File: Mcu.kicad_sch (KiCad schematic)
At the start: 28 parts, among them J10 AUX2, J8 AUX0, J9 AUX1, U7 STM32H723VGHx, X2 X322516MLB4SI

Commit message: Started discrete inverter version
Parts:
- added U12: STM32H723VGT6, LQFP100_STM, symbol 2026-08-10_19-26-15:STM32H723VGT6
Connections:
- net AN_DRV_SO_A: now also U12.30 (PA6); no longer U7.J3 (PA6)
- net AN_DRV_SO_B: now also U12.31 (PA7); no longer U7.K3 (PA7)
- net AN_DRV_SO_C: now also U12.35 (PB1); no longer U7.K4 (PB1)
- net AN_EXT_IN_0: now also U12.25 (PA3); no longer U7.K2 (PA3)
- net AN_EXT_IN_1: now also U12.15 (PC0); no longer U7.F1 (PC0)
- net AN_VBUS: now also U12.24 (PA2); no longer U7.J2 (PA2)
- net CAN_RX: now also U12.81 (PD0); no longer U7.D8 (PD0)
- net CAN_TX: now also U12.82 (PD1); no longer U7.E8 (PD1)
- net DEBUG_RX: now also U12.80 (PC12); no longer U7.C8 (PC12)
- net DEBUG_TX: now also U12.83 (PD2); no longer U7.B7 (PD2)
- net DRV_AN_REF: now also U12.16 (PC1); no longer U7.F2 (PC1)
- net DRV_OFF: now also U12.47 (PB11); no longer U7.K7 (PB11)
- net DRV_SPI_CLK: now also U12.84 (PD3); no longer U7.C7 (PD3)
- net DRV_SPI_SDI: now also U12.18 (PC3_C); no longer U7.F3 (PC3_C)
- net DRV_SPI_SDO: now also U12.17 (PC2_C); no longer U7.E2 (PC2_C)
- net DRV_SPI_~{SCS}: now also U12.96 (PB9); no longer U7.A4 (PB9)
- net ENC_CLK: now also U12.89 (PB3); no longer U7.A7 (PB3(JTDO)
- net ENC_CS: now also U12.28 (PA4); no longer U7.G3 (PA4)
- net ENC_MISO: now also U12.90 (PB4); no longer U7.A6 (PB4(NJTRST))
- net ENC_MOSI: now also U12.91 (PB5); no longer U7.C5 (PB5)
- net GND: now also U12.10 (VSS), U12.26 (VSS); no longer U7.C2 (VSS), U7.E4 (VSS), U7.E5 (VSS), U7.E6 (VSS), U7.G1 (VSSA), U7.J1 (VSS)
- net NRST: now also U12.14 (NRST); no longer U7.E1 (NRST)
- net PA10: now also U12.69 (PA10); no longer U7.D10 (PA10)
- net PA5: now also U12.29 (PA5); no longer U7.H3 (PA5)
- net PA8: now also U12.67 (PA8); no longer U7.D9 (PA8)
- net PA9: now also U12.68 (PA9); no longer U7.C9 (PA9)
- net PB10: now also U12.46 (PB10); no longer U7.J7 (PB10)
- net PB12: now also U12.51 (PB12); no longer U7.K8 (PB12)
- net PB13: now also U12.52 (PB13); no longer U7.J8 (PB13)
- net PB14: now also U12.53 (PB14); no longer U7.H10 (PB14)
- net PB15: now also U12.54 (PB15); no longer U7.G10 (PB15)
- net PB6: now also U12.92 (PB6); no longer U7.B5 (PB6)
- net PB7: now also U12.93 (PB7); no longer U7.A5 (PB7)
- net PB8: now also U12.95 (PB8); no longer U7.B4 (PB8)
- net PC13: now also U12.7 (PC13); no longer U7.A2 (PC13)
- net PC14: now also U12.8 (PC14-OSC32_IN); no longer U7.A1 (PC14)
- net PC15: now also U12.9 (PC15-OSC32_OUT); no longer U7.B1 (PC15)
- net PC4: now also U12.32 (PC4); no longer U7.G4 (PC4)
- net PC5: now also U12.33 (PC5); no longer U7.H4 (PC5)
- net PC6: now also U12.63 (PC6); no longer U7.F10 (PC6)
- net PC7: now also U12.64 (PC7); no longer U7.E10 (PC7)
- net PC8: now also U12.65 (PC8); no longer U7.F9 (PC8)
- net PC9: now also U12.66 (PC9); no longer U7.E9 (PC9)
- net PD10: now also U12.57 (PD10); no longer U7.H9 (PD10)
- net PD11: now also U12.58 (PD11); no longer U7.G9 (PD11)
- net PD12: now also U12.59 (PD12); no longer U7.K10 (PD12)
- net PD13: now also U12.60 (PD13); no longer U7.J10 (PD13)
- net PD14: now also U12.61 (PD14); no longer U7.H8 (PD14)
- net PD15: now also U12.62 (PD15); no longer U7.G8 (PD15)
- net PD4: now also U12.85 (PD4); no longer U7.D7 (PD4)
- net PD5: now also U12.86 (PD5); no longer U7.B6 (PD5)
- net PD6: now also U12.87 (PD6); no longer U7.C6 (PD6)
- net PD7: now also U12.88 (PD7); no longer U7.D6 (PD7)
- net PD8: now also U12.55 (PD8); no longer U7.K9 (PD8)
- net PD9: now also U12.56 (PD9); no longer U7.J9 (PD9)
- net PE0: now also U12.97 (PE0); no longer U7.D4 (PE0)
- net PE1: now also U12.98 (PE1); no longer U7.C4 (PE1)
- net PE14: now also U12.44 (PE14); no longer U7.G7 (PE14)
- net PE15: now also U12.45 (PE15); no longer U7.H7 (PE15)
- net PE5: now also U12.4 (PE5); no longer U7.D3 (PE5)
- net PE6: now also U12.5 (PE6); no longer U7.E3 (PE6)
- net PE7: now also U12.37 (PE7); no longer U7.H5 (PE7)
- net PWM_A_H: now also U12.39 (PE9); no longer U7.K5 (PE9)
- net PWM_A_L: now also U12.38 (PE8); no longer U7.J5 (PE8)
- net PWM_B_H: now also U12.41 (PE11); no longer U7.H6 (PE11)
- net PWM_B_L: now also U12.40 (PE10); no longer U7.G6 (PE10)
- net PWM_C_H: now also U12.43 (PE13); no longer U7.K6 (PE13)
- net PWM_C_L: now also U12.42 (PE12); no longer U7.J6 (PE12)
- net QUAD_ENC_A: now also U12.22 (PA0); no longer U7.G2 (PA0)
- net QUAD_ENC_B: now also U12.23 (PA1); no longer U7.H2 (PA1)
- net RS485_DE: now also U12.77 (PA15); no longer U7.A8 (PA15(JTDI))
- net RS485_DI: now also U12.78 (PC10); no longer U7.B9 (PC10)
- net RS485_RO: now also U12.79 (PC11); no longer U7.B8 (PC11)
- net SWD_CLK: now also U12.76 (PA14); no longer U7.A9 (PA14(JTCK)
- net SWD_DATA: now also U12.72 (PA13); no longer U7.A10 (PA13(JTMS)
- net UI_LED_BLUE: now also U12.1 (PE2); no longer U7.A3 (PE2)
- net UI_LED_RED: now also U12.2 (PE3); no longer U7.B3 (PE3)
- net UI_LED_YELLOW: now also U12.3 (PE4); no longer U7.C3 (PE4)
- net USB+: now also U12.71 (PA12); no longer U7.B10 (PA12)
- net USB-: now also U12.70 (PA11); no longer U7.C10 (PA11)
- net ~{DRV_FAULT}: now also U12.34 (PB0); no longer U7.J4 (PB0)
- net ~{DRV_SLEEP}: now also U12.36 (PB2); no longer U7.G5 (PB2)
- net at C8.1, X2.1 (OSC): now also U12.13 (PH1-OSC_OUT); no longer U7.D1 (PH1)
- net at C9.1, X2.3 (OSC): now also U12.12 (PH0-OSC_IN); no longer U7.C1 (PH0)
- net at R26.2: now also U12.94 (BOOT0); no longer U7.D5 (BOOT0)
- net at C2.1: now also U12.48 (VCAP); no longer U7.E7 (VCAP)
- net at C1.1: now also U12.73 (VCAP); no longer U7.F8 (VCAP)
- new net: U7.C2 (VSS), U7.E4 (VSS), U7.E5 (VSS), U7.E6 (VSS), U7.J1 (VSS)
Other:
- moved on the sheet: C1, C2, C3, C8, C9, D4, D6, D7, J10, J8, J9, R26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

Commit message: added drv8353, stm32h723vgt6
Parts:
- removed R25: 10kΩ, PCM_JLCPCB:R_0603, symbol PCM_JLCPCB-Resistors:0603,10kΩ
- removed U7: STM32H723VGHx, Package_BGA:TFBGA-100_8x8mm_Layout10x10_P0.8mm, symbol MCU_ST_STM32H7:STM32H723VGHx
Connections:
- net +3.3V: now also U12.100 (VDD), U12.11 (VDD), U12.27 (VDD), U12.50 (VDD), U12.6 (VBAT), U12.75 (VDD)
- net GND: now also U12.19 (VSSA), U12.49 (VSS), U12.74 (VSS), U12.99 (VSS)
- net at U12.20 (VREF+): now also C28.1, C29.1, FB2.2, U12.21 (VDDA)
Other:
- moved on the sheet: C1, C2, C28, C29, C3, C30, C31, C32, C33, C34, C35, C36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

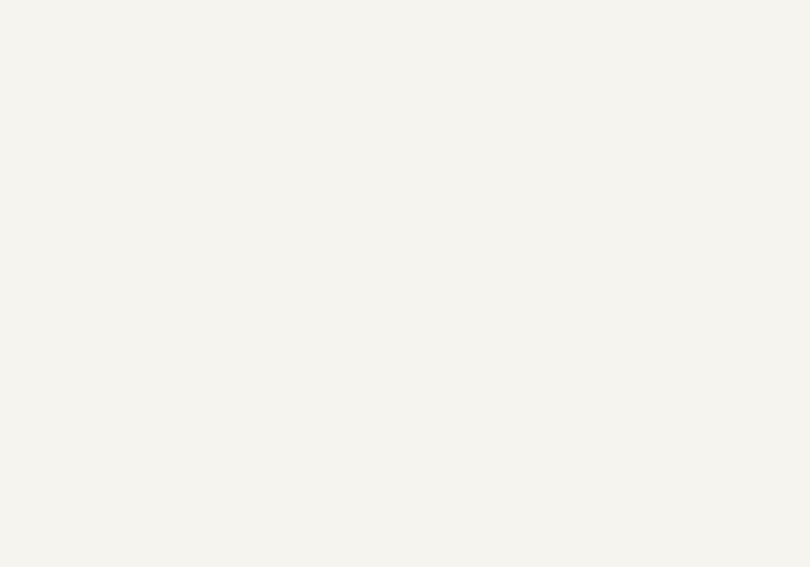
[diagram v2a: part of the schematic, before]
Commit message: Circular pcb edge cut
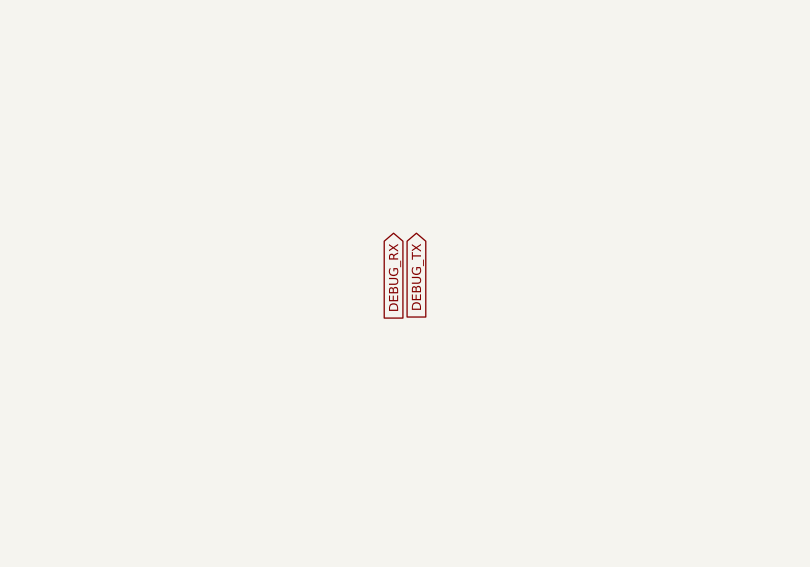
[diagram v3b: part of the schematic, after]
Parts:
- J8, J9: footprint Connector_PinSocket_2.54mm:PinSocket_2x10_P2.54mm_Vertical -> Connector_PinSocket_1.27mm:PinSocket_2x10_P1.27mm_Vertical
- U12: footprint LQFP100_STM -> Package_QFP:LQFP-100_14x14mm_P0.5mm
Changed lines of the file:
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@@
 		)
 	)
+	(global_label "DEBUG_TX"
+		(shape input)
+		(at 144.78 86.36 270)
+		(fields_autoplaced yes)
+		(effects
+			(font
+				(size 1.016 1.016)
+			)
+			(justify right)
+		)
+		(property "Intersheetrefs" "${INTERSHEET_REFS}"
+			(at 144.78 96.2953 90)
+			(effects
+				(font
+					(size 1.27 1.27)
+				)
+				(justify right)
+				(hide yes)
+			)
+		)
+	)
 	(global_label "AN_DRV_SO_A"
 		(shape input)
@@
 		)
 	)
+	(global_label "DEBUG_RX"
+		(shape input)
+		(at 142.24 86.36 270)
+		(fields_autoplaced yes)
+		(effects
+			(font
+				(size 1.016 1.016)
+			)
+			(justify right)
+		)
+		(property "Intersheetrefs" "${INTERSHEET_REFS}"
+			(at 142.24 96.5372 90)
+			(effects
+				(font
+					(size 1.27 1.27)
+				)
+				(justify right)
+				(hide yes)
+			)
+		)
+	)
 	(global_label "~{DRV_FAULT}"
 		(shape output)
@@
 			)
 		)
-		(property "Footprint" "LQFP100_STM"
+		(property "Footprint" "Package_QFP:LQFP-100_14x14mm_P0.5mm"
 			(at 105.156 219.456 0)
 			(effects
@@
 			)
 		)
-		(property "Footprint" "Connector_PinSocket_2.54mm:PinSocket_2x10_P2.54mm_Vertical"
+		(property "Footprint" "Connector_PinSocket_1.27mm:PinSocket_2x10_P1.27mm_Vertical"
 			(at 71.12 43.18 0)
 			(effects
@@
 			)
 		)
-		(property "Footprint" "Connector_PinSocket_2.54mm:PinSocket_2x10_P2.54mm_Vertical"
+		(property "Footprint" "Connector_PinSocket_1.27mm:PinSocket_2x10_P1.27mm_Vertical"
 			(at 38.1 43.18 0)
 			(effects
@@
 			)
 		)
-		(property "Footprint" "LQFP100_STM"
+		(property "Footprint" "Package_QFP:LQFP-100_14x14mm_P0.5mm"
 			(at 263.906 54.356 0)
 			(effects
@@
 			)
 		)
-		(property "Footprint" "LQFP100_STM"
+		(property "Footprint" "Package_QFP:LQFP-100_14x14mm_P0.5mm"
 			(at 265.176 148.336 0)
 			(effects

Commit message: Placement, some layout
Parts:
- FB2: value ~ -> (none)

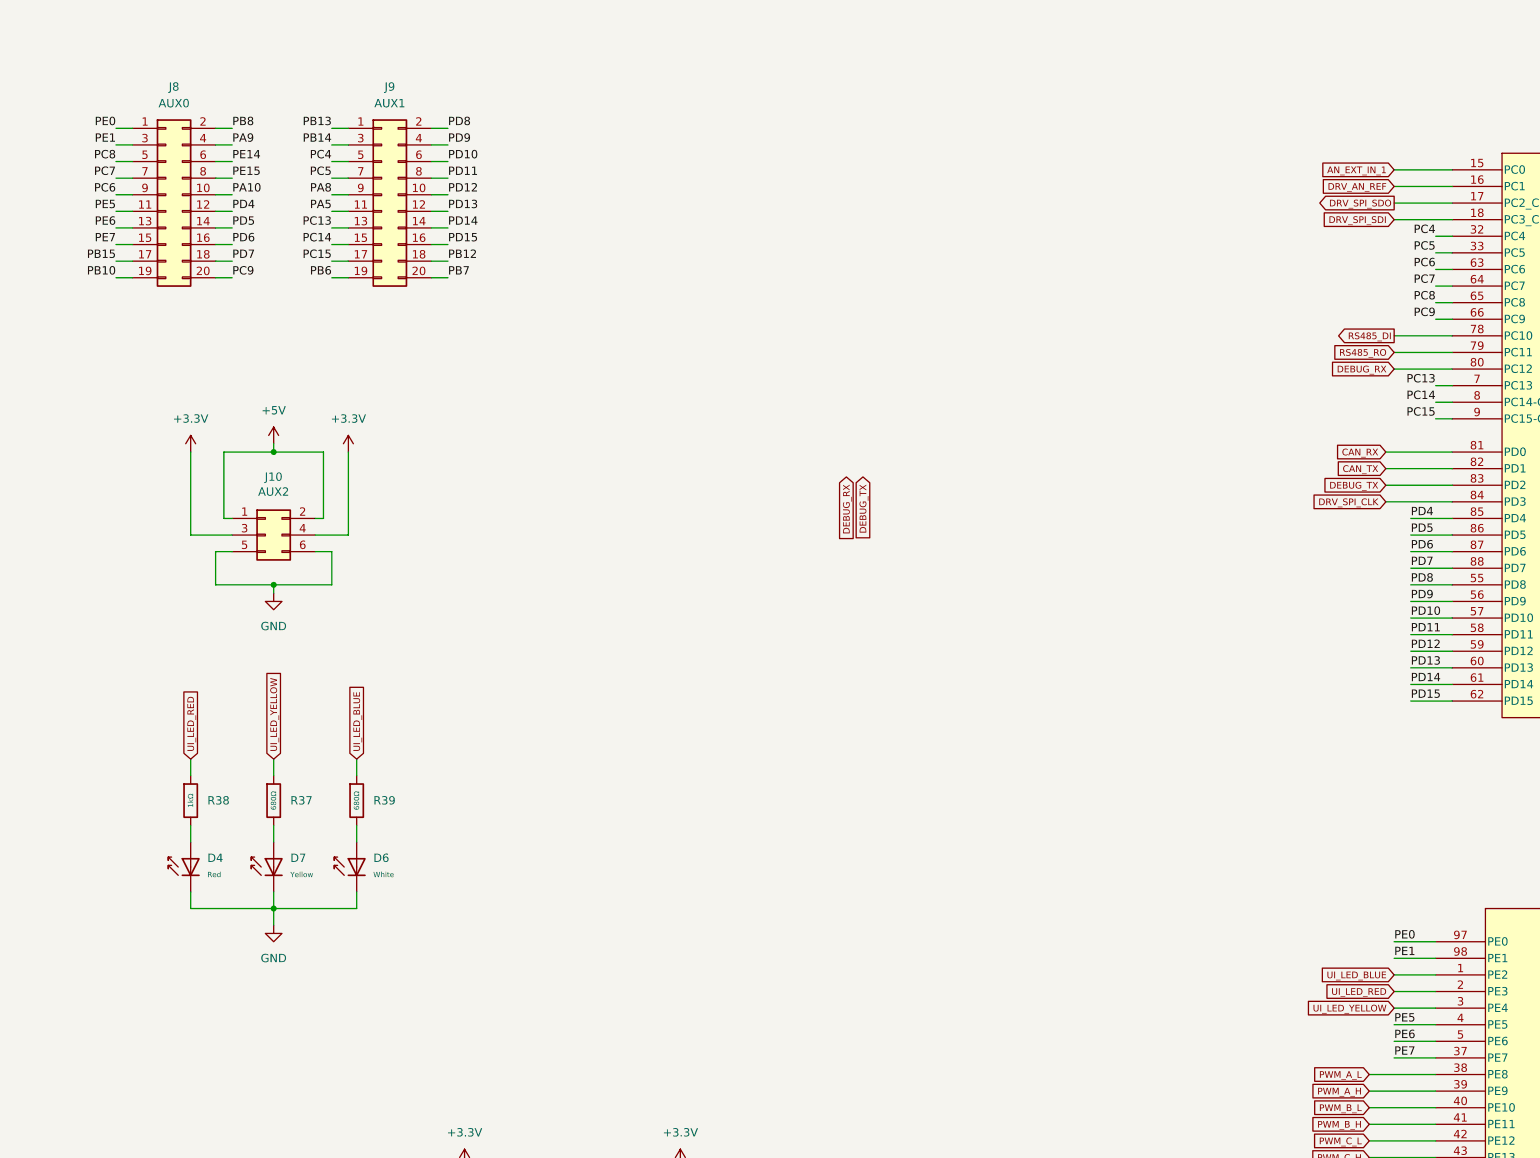
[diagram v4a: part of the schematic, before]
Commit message: More layout, add can,rs485 leds
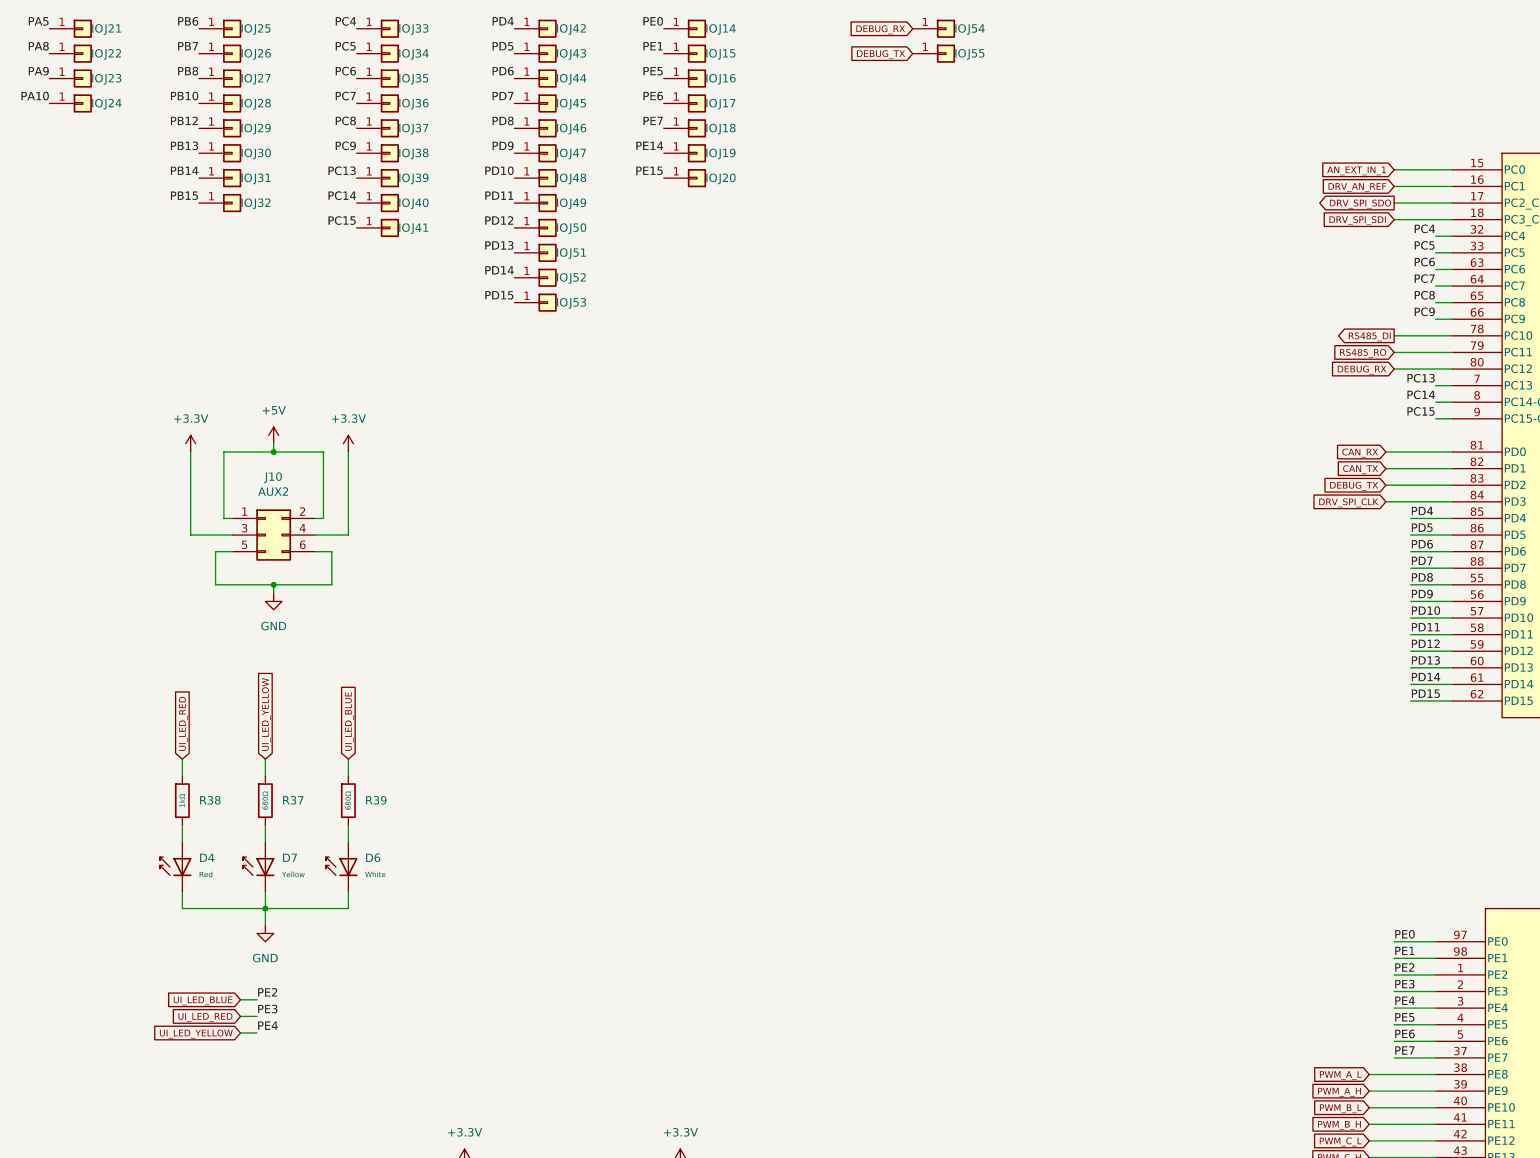
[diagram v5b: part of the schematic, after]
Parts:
- removed J8: AUX0, Connector_PinSocket_1.27mm:PinSocket_2x10_P1.27mm_Vertical, symbol Connector_Generic:Conn_02x10_Odd_Even
- removed J9: AUX1, Connector_PinSocket_1.27mm:PinSocket_2x10_P1.27mm_Vertical, symbol Connector_Generic:Conn_02x10_Odd_Even
- added J14, J15, J16, J17, J18, J19, J20, J21, J22, J23, J24, J25, J26, J27, J28, J29, J30, J31, J32, J33, J34, J35, J36, J37, J38, J39, J40, J41, J42, J43, J44, J45, J46, J47, J48, J49, J50, J51, J52, J53, J54, J55: IO, TestPoint:TestPoint_THTPad_D1.0mm_Drill0.5mm, symbol Connector_Generic:Conn_01x01
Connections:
- net DEBUG_RX: now also J54.1 (Pin_1)
- net DEBUG_TX: now also J55.1 (Pin_1)
- net PA10: now also J24.1 (Pin_1)
- net PA5: now also J21.1 (Pin_1)
- net PA8: now also J22.1 (Pin_1)
- net PA9: now also J23.1 (Pin_1)
- net PB10: now also J28.1 (Pin_1)
- net PB12: now also J29.1 (Pin_1)
- net PB13: now also J30.1 (Pin_1)
- net PB14: now also J31.1 (Pin_1)
- net PB15: now also J32.1 (Pin_1)
- net PB6: now also J25.1 (Pin_1)
- net PB7: now also J26.1 (Pin_1)
- net PB8: now also J27.1 (Pin_1)
- net PC13: now also J39.1 (Pin_1)
- net PC14: now also J40.1 (Pin_1)
- net PC15: now also J41.1 (Pin_1)
- net PC4: now also J33.1 (Pin_1)
- net PC5: now also J34.1 (Pin_1)
- net PC6: now also J35.1 (Pin_1)
- net PC7: now also J36.1 (Pin_1)
- net PC8: now also J37.1 (Pin_1)
- net PC9: now also J38.1 (Pin_1)
- net PD10: now also J48.1 (Pin_1)
- net PD11: now also J49.1 (Pin_1)
- net PD12: now also J50.1 (Pin_1)
- net PD13: now also J51.1 (Pin_1)
- net PD14: now also J52.1 (Pin_1)
- net PD15: now also J53.1 (Pin_1)
- net PD4: now also J42.1 (Pin_1)
- net PD5: now also J43.1 (Pin_1)
- net PD6: now also J44.1 (Pin_1)
- net PD7: now also J45.1 (Pin_1)
- net PD8: now also J46.1 (Pin_1)
- net PD9: now also J47.1 (Pin_1)
- net PE0: now also J14.1 (Pin_1)
- net PE1: now also J15.1 (Pin_1)
- net PE14: now also J19.1 (Pin_1)
- net PE15: now also J20.1 (Pin_1)
- net PE5: now also J16.1 (Pin_1)
- net PE6: now also J17.1 (Pin_1)
- net PE7: now also J18.1 (Pin_1)
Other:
- moved on the sheet: D4, D6, D7, R37, R38, R39

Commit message: Layout 90%.
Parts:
- added J56: IO, TestPoint:TestPoint_THTPad_D1.0mm_Drill0.5mm, symbol Connector_Generic:Conn_01x01
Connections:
- net DEBUG_RX: no longer J54.1 (Pin_1)
- net DEBUG_TX: no longer J55.1 (Pin_1)
- net DRV_AN_REF renamed PC1
- net PC1: now also J56.1 (Pin_1)
- net PE14 renamed CAN_ACT
- net PE15 renamed RS485_ACT
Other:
- moved on the sheet: J33, J34, J35, J36, J37, J38, J39, J40, J41
